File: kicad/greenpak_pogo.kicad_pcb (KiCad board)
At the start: 2 copper layers, 7.6 x 14.4 mm, 5 parts

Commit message: Cleaned up post project name change to greenpak_pogo.
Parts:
- G*: footprint pogo:QWIIC_logo_6mm -> greenpak_pogo:QWIIC_logo_6mm
- REF**: footprint pogo:JST_SH_SM04B-SRSS-TB_1x04-1MP_P1.00mm_Horizontal -> greenpak_pogo:JST_SH_SM04B-SRSS-TB_1x04-1MP_P1.00mm_Horizontal
- REF**: value POGO_PINS -> GREENPAK_POGO_PINS; footprint pogo:POGO_PINS -> greenpak_pogo:GREENPAK_POGO_PINS
- REF**: footprint pogo:SOLDER_JUMPER -> greenpak_pogo:SOLDER_JUMPER
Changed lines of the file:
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@@
   )
   (net 0 "")
-  (footprint "pogo:JST_SH_SM04B-SRSS-TB_1x04-1MP_P1.00mm_Horizontal" locked (layer "F.Cu")
+  (footprint "greenpak_pogo:JST_SH_SM04B-SRSS-TB_1x04-1MP_P1.00mm_Horizontal" locked (layer "F.Cu")
     (at 0 7.8232)
     (descr "JST SH series connector, SM04B-SRSS-TB (http://www.jst-mfg.com/product/pdf/eng/eSH.pdf), generated with kicad-footprint-generator")
@@
     (pad "3" thru_hole roundrect locked (at 0.5 -2) (size 0.6 1.55) (drill 0.3) (layers "*.Cu" "F.Paste" "F.Mask") (roundrect_rratio 0.25))
     (pad "4" thru_hole roundrect locked (at 1.5 -2) (size 0.6 1.55) (drill 0.3) (layers "*.Cu" "F.Paste" "F.Mask") (roundrect_rratio 0.25))
-    (pad "MP" thru_hole roundrect locked (at -2.8 1.875) (size 1.2 1.8) (drill 0.3) (layers "*.Cu" "F.Paste" "F.Mask") (roundrect_rratio 0.2083333333))
-    (pad "MP" thru_hole roundrect locked (at 2.8 1.875) (size 1.2 1.8) (drill 0.3) (layers "*.Cu" "F.Paste" "F.Mask") (roundrect_rratio 0.2083333333))
+    (pad "MP" thru_hole roundrect locked (at -2.8 1.875) (size 1.2 1.8) (drill 0.3) (layers "*.Cu" "F.Paste" "F.Mask") (roundrect_rratio 0.208333))
+    (pad "MP" thru_hole roundrect locked (at 2.8 1.875) (size 1.2 1.8) (drill 0.3) (layers "*.Cu" "F.Paste" "F.Mask") (roundrect_rratio 0.208333))
     (model "${KIPRJMOD}/3d_models/SM4B-SRSS-TB.step"
       (offset (xyz -1.5 1.7 0))
@@
     )
   )
-  (footprint "pogo:POGO_PINS" locked (layer "F.Cu")
+  (footprint "greenpak_pogo:GREENPAK_POGO_PINS" locked (layer "F.Cu")
     (at 0 0)
     (descr "Through hole straight pin header, 1x01, 2.54mm pitch, single row")
@@
         (effects (font (size 1 1) (thickness 0.15)))
     )
-    (fp_text value "POGO_PINS" (at 0 2.33) (layer "F.Fab") hide
+    (fp_text value "GREENPAK_POGO_PINS" (at 0 2.33) (layer "F.Fab") hide
         (effects (font (size 1 1) (thickness 0.15)))
     )
@@
     )
   )
-  (footprint "pogo:SOLDER_JUMPER" (layer "F.Cu")
+  (footprint "greenpak_pogo:SOLDER_JUMPER" (layer "F.Cu")
     (at 0 3.556)
     (descr "SMD Solder Jumper, 1x1.5mm Pads, 0.3mm gap, open")
@@
     (pad "2" smd rect (at 0.65 0) (size 1 1.5) (layers "F.Cu" "F.Mask"))
   )
-  (footprint "pogo:QWIIC_logo_6mm" (layer "B.Cu")
+  (footprint "greenpak_pogo:QWIIC_logo_6mm" (layer "B.Cu")
     (at 0.040263 4.7302 180)
     (attr board_only exclude_from_pos_files exclude_from_bom)

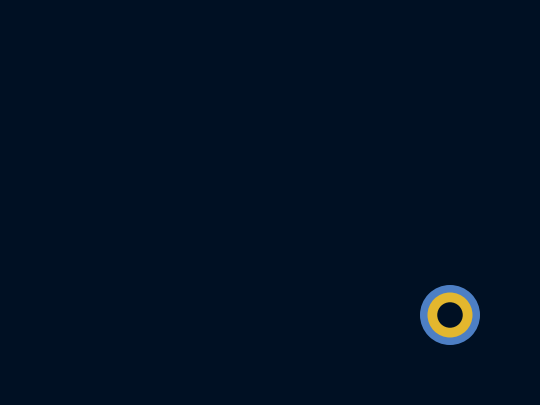
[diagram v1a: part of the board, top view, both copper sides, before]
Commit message: Added 3D models.
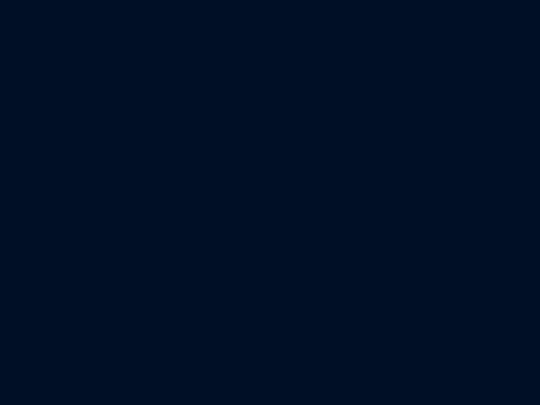
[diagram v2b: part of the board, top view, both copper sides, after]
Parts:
- removed the REF** at (160.0, 79.4)
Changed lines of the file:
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@@
-    )
-  )
-  (footprint "pogo:POGO_PIN" (layer "F.Cu")
-    (at 160.02 79.375)
-    (descr "Through hole straight pin header, 1x01, 2.54mm pitch, single row")
-    (tags "Through hole pin header THT 1x01 2.54mm single row")
-    (attr through_hole)
-    (fp_text reference "REF**" (at 0 -2.33) (layer "F.SilkS") hide
-        (effects (font (size 1 1) (thickness 0.15)))
-    )
-    (fp_text value "POGO_PIN" (at 0 2.33) (layer "F.Fab") hide
-        (effects (font (size 1 1) (thickness 0.15)))
-    )
-    (fp_circle (center 0 0) (end 0.85 0)
-      (stroke (width 0.3) (type solid)) (fill none) (layer "B.Cu"))
-    (fp_circle (center 0 0) (end 0.85 0)
-      (stroke (width 0.3) (type solid)) (fill none) (layer "B.Mask"))
-    (pad "1" thru_hole circle (at 0 0) (size 1.5 1.5) (drill 0.85) (layers "*.Cu" "*.Mask"))
-    (model "${KICAD6_3DMODEL_DIR}/Connector_PinHeader_2.54mm.3dshapes/PinHeader_1x01_P2.54mm_Vertical.wrl"
-      (offset (xyz 0 0 0))
-      (scale (xyz 1 1 1))
-      (rotate (xyz 0 0 0))
     )
   )
